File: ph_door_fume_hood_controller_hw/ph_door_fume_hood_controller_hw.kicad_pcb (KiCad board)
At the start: 2 copper layers, 145.7 x 133.3 mm, 249 parts, among them IC1 6N137, IC2 6N137, J1 Conn_01x03, J10 Conn_01x03, J11 Conn_01x02, J12 Conn_01x06, J13 Conn_01x02, J14 Conn_01x03, J15 Conn_01x03, J2 Conn_01x04, J3 CONN_01X04, J4 Conn_01x03, J5 Conn_01x03, J6 Conn_01x02, J7 Conn_01x06, J8 USB_OTG, J9 Conn_01x02, M1 DC-DC-24-12V-200mA, M2 MORSUN_485, Q1 C1815, Q10 A1015, Q11 Q_NMOS_GDS, Q2 Q_PMOS_GDS, Q3 Q_NMOS_GDS, Q4 Q_NMOS_GDS, Q5 C1815, Q6 Q_NMOS_GDS, Q7 Q_NMOS_GDS, Q8 C1815, Q9 Q_NMOS_GDS, U1 74HC123, U10 PC817, U11 MCP4725, U12 ASM1117-3V3, U13 PC817, U14 PC817, U15 LM358, U16 PC817, U17 PC817, U18 PC817, U19 PC817, U2 AD8601, U20 PC817, U21 PC817, U22 PC817, U23 PC817, U3 PC817, U4 PC817, U5 TB6600, U6 PC817, U7 STM32F103C8, U8 ASM1117, U9 XL4015, Y1 Crystal, Y2 32768Mhz

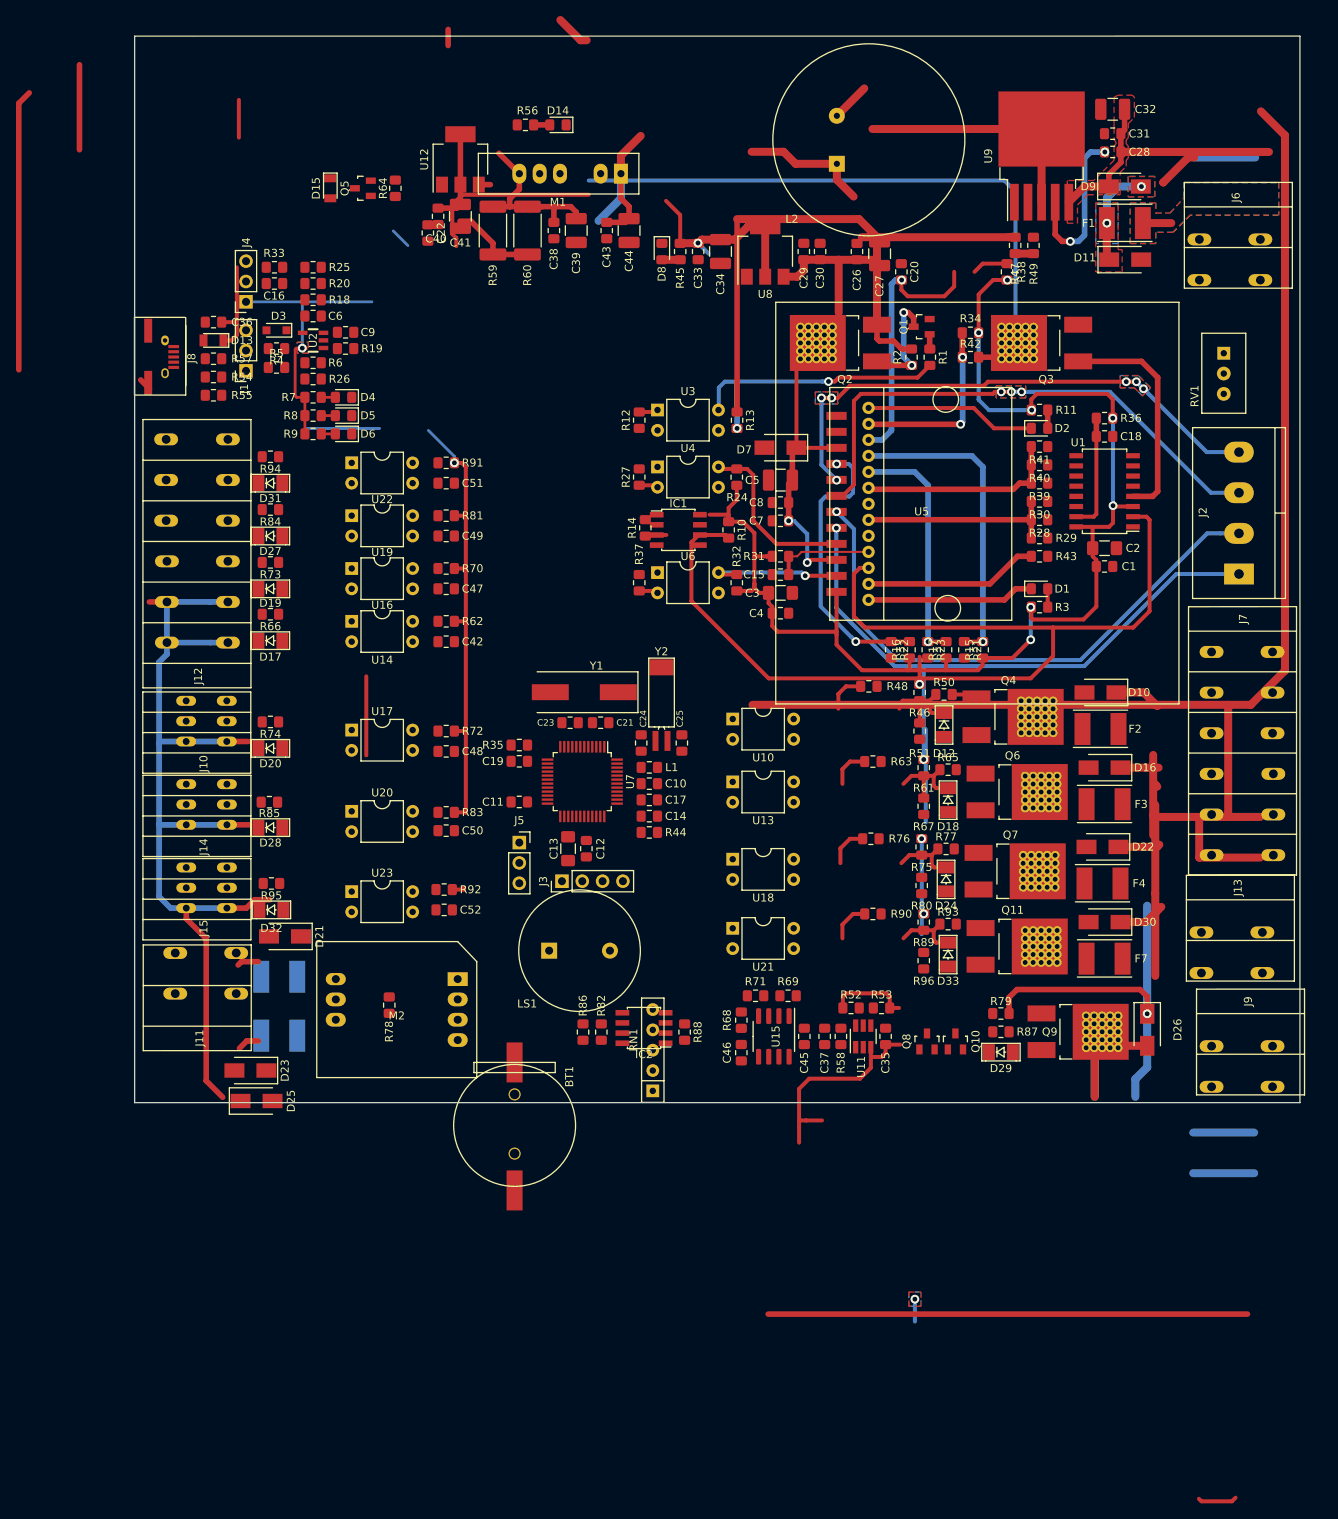
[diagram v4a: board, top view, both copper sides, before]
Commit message: door_fume_hood
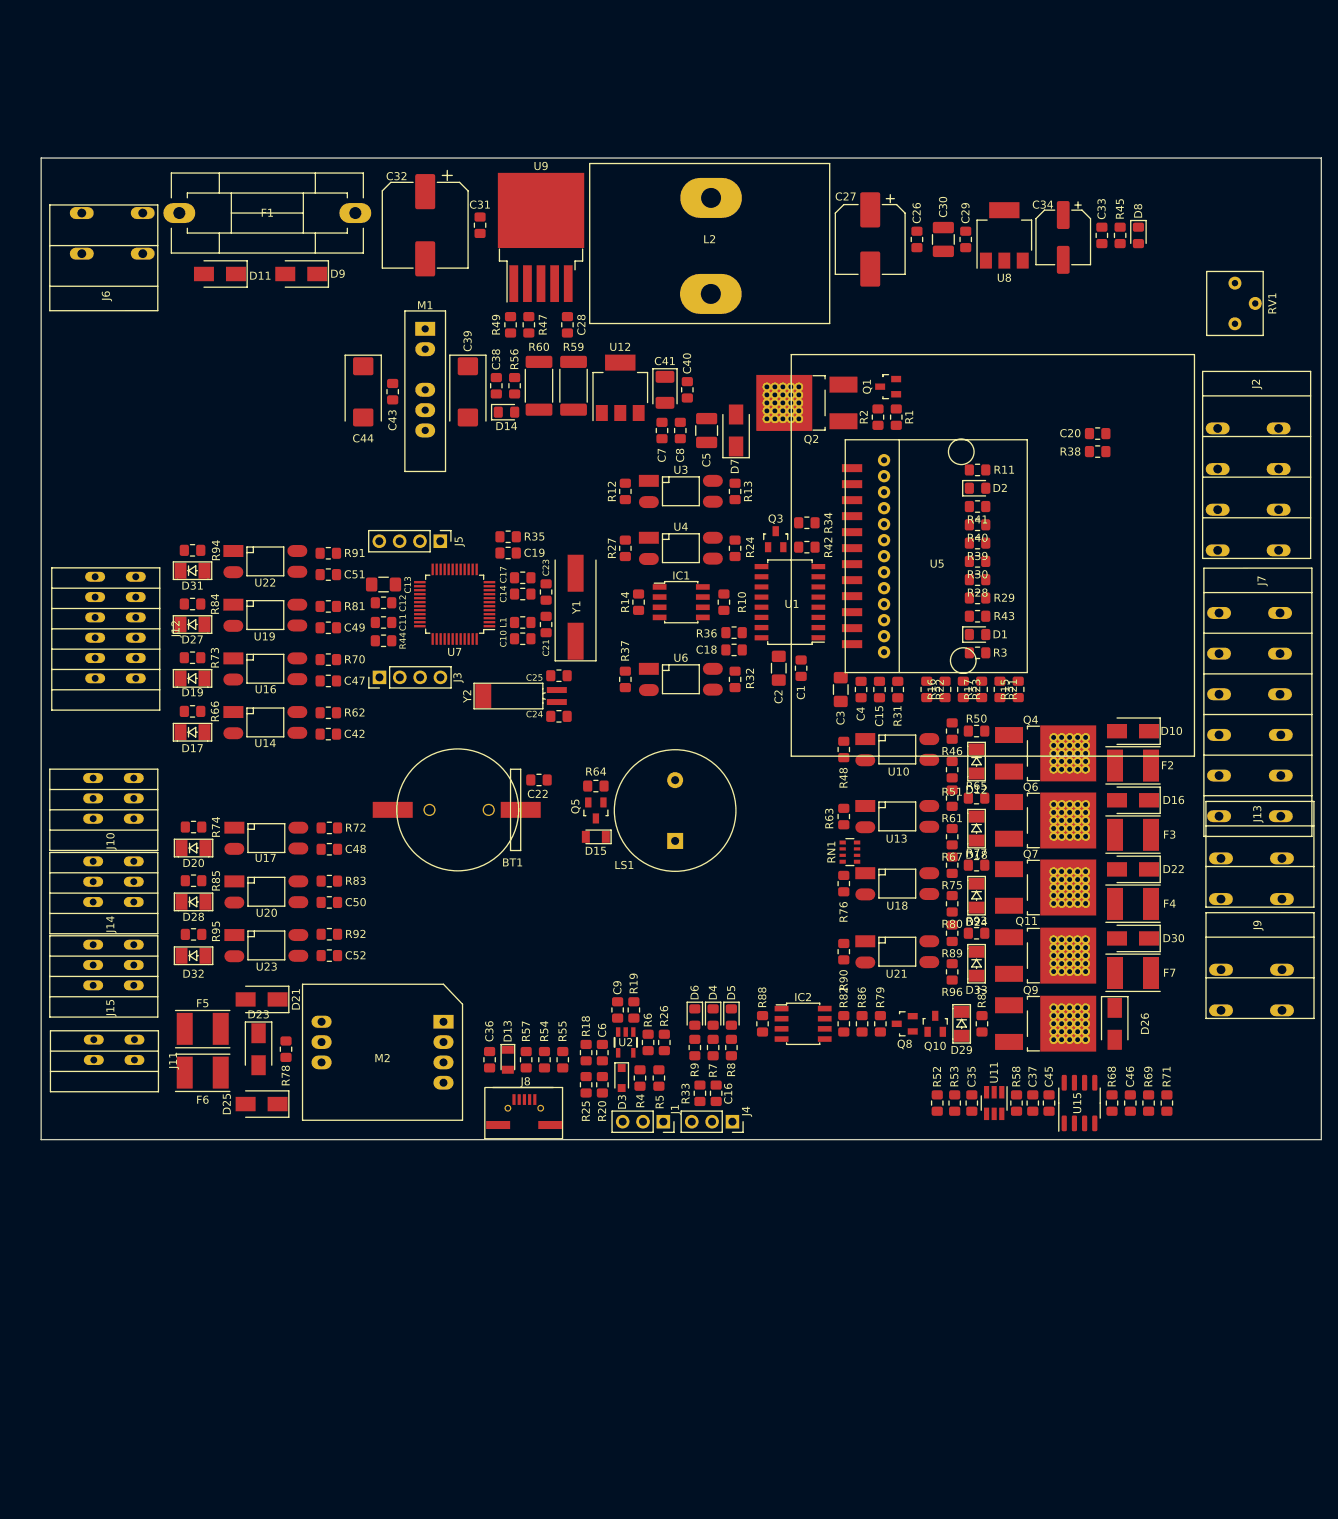
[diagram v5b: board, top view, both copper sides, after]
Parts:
- C27: footprint Capacitor_SMD:C_1210_3225Metric_Pad1.42x2.65mm_HandSolder -> Capacitor_SMD:CP_Elec_8x10.5
- C30: value 10uF -> 10uF/25V; footprint Capacitor_SMD:C_0805_2012Metric_Pad1.15x1.40mm_HandSolder -> Capacitor_SMD:C_1210_3225Metric_Pad1.42x2.65mm_HandSolder
- C32: value 220uF/50V -> 470uF/50V; footprint Capacitor_SMD:C_1210_3225Metric_Pad1.42x2.65mm_HandSolder -> Capacitor_SMD:CP_Elec_10x14.3
- C34: footprint Capacitor_SMD:C_1210_3225Metric_Pad1.42x2.65mm_HandSolder -> Capacitor_SMD:CP_Elec_6.3x5.4
- C39: value 330uF/25V -> 100uF/25V; footprint Capacitor_SMD:C_1210_3225Metric_Pad1.42x2.65mm_HandSolder -> Capacitor_Tantalum_SMD:CP_EIA-7343-20_Kemet-V_Pad2.25x2.55mm_HandSolder
- C41: value 47uF -> 100uF/10V; footprint Capacitor_SMD:C_1210_3225Metric_Pad1.42x2.65mm_HandSolder -> Capacitor_Tantalum_SMD:CP_EIA-3528-15_AVX-H_Pad1.50x2.35mm_HandSolder
- C44: value 330uF/25V -> 100uF/50V; footprint Capacitor_SMD:C_1210_3225Metric_Pad1.42x2.65mm_HandSolder -> Capacitor_Tantalum_SMD:CP_EIA-7343-31_Kemet-D_Pad2.25x2.55mm_HandSolder
- F1: footprint VinhTho_Lib:Fuse_SMD1812 -> VinhTho_Lib:Fuseholder5x20_horiz_SemiClosed_Casing10x25mm
- F5, F6: moved to F.Cu
- J11: footprint VinhTho_Lib:TerminalBlock_WAGO-236_2Stift_R5mm_2pol -> VinhTho_Lib:TerminalBlock_WAGO_2.54mm_2P
- J12: footprint VinhTho_Lib:TerminalBlock-WAGO-6P -> VinhTho_Lib:TerminalBlock_WAGO_2.54mm_6P
- J2: footprint VinhTho_Lib:Domino-5.08mm_4pol -> VinhTho_Lib:TerminalBlock_WAGO-236_2Stift_R5mm_4pol
- J5: value Conn_01x03 -> Conn_01x04; footprint Connector_PinSocket_2.54mm:PinSocket_1x03_P2.54mm_Vertical -> Connector_PinHeader_2.54mm:PinHeader_1x04_P2.54mm_Vertical
- L2: footprint VinhTho_Lib:L181-5A -> VinhTho_Lib:Inductor_5A
- Q3: value Q_NMOS_GDS -> Q_NMOS_GSD; footprint VinhTho_Lib:TO-252-2 -> VinhTho_Lib:SOT-23
- RN1: value R_Network04 -> R_Pack04; footprint Resistor_THT:R_Array_SIP5 -> Resistor_SMD:R_Array_Convex_4x0603
- RV1: footprint VinhTho_Lib:VR1 -> VinhTho_Lib:VR-3362P
- U10, U13, U14, U16, U17, U18, U19, U20, U21, U22, U23, U3, U4, U6: footprint Package_DIP:DIP-4_W7.62mm -> VinhTho_Lib:Optocoupler_SMD
- moved J6 147.3 mm to (66.0, 46.7), turned to 90 degrees
- moved J4 119.2 mm to (147.4, 155.2), turned to 270 degrees
- moved F1 118.2 mm to (78.2, 41.7), turned to 0 degrees
- moved R33 116.1 mm to (143.3, 151.7), turned to 270 degrees
- moved C16 115.3 mm to (145.3, 151.7), turned to 90 degrees
- moved D11 113.2 mm to (83.3, 49.3), turned to 180 degrees
- moved R25 107.7 mm to (129.1, 150.6), turned to 90 degrees
- moved J1 107.4 mm to (138.7, 155.2), turned to 270 degrees
- moved R20 106.5 mm to (131.1, 150.6), turned to 270 degrees
- moved J8 105.1 mm to (119.3, 153.6), turned to 0 degrees
- moved D9 103.5 mm to (93.5, 49.3), turned to 180 degrees
- moved D3 102.9 mm to (133.5, 149.8), turned to 270 degrees
- moved R4 101.9 mm to (135.8, 149.8), turned to 90 degrees
- moved R5 100.9 mm to (138.2, 149.8), turned to 90 degrees
- moved R18 100.1 mm to (129.1, 146.6), turned to 270 degrees
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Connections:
- J5 pad 1: /TX -> +3V3
- J5 pad 2: /RX -> GND
- J5 pad 3: GND -> /TX
- Q3 pad 2: Net-(Q3-Pad2) -> GNDPWR
- Q3 pad 3: GNDPWR -> Net-(Q3-Pad3)
- R42 pad 2: Net-(Q3-Pad2) -> Net-(Q3-Pad3)
- RN1 pad 2: /O4 -> GND
- RN1 pad 3: /O3 -> GND
- RN1 pad 4: /O2 -> GND
- RN1 pad 5: /O1 -> /O4
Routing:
- net +24V: track 583.2 -> 0.00 mm, vias 5 -> 0
- net +5V: track 272.2 -> 0.00 mm, vias 8 -> 0
- net +3V3: track 194.9 -> 0.00 mm, vias 3 -> 0
- net /CLK: track 126.0 -> 0.00 mm
- net +12V: track 116.1 -> 0.00 mm
- net Net-(J2-Pad2): track 71.0 -> 0.00 mm, vias 1 -> 0
- net Net-(J2-Pad1): track 68.1 -> 0.00 mm, vias 1 -> 0
- net Net-(J2-Pad4): track 67.7 -> 0.00 mm, vias 6 -> 0
- net Net-(J2-Pad3): track 67.0 -> 0.00 mm, vias 3 -> 0
- net Net-(C5-Pad1): track 41.2 -> 0.00 mm, vias 2 -> 0
- net /M1: track 39.1 -> 0.00 mm, vias 1 -> 0
- net GND: track 36.7 -> 0.00 mm
- net /PWR_STEP: track 36.2 -> 0.00 mm, vias 2 -> 0
- net /M2: track 35.9 -> 0.00 mm, vias 2 -> 0
- net Net-(L2-Pad2): track 35.1 -> 0.00 mm
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- removed copper zone on F.Cu, net +24V
- removed copper zone on B.Cu, net +3V3
- removed copper zone on F.Cu, net +3V3
- removed copper zone on B.Cu, net Net-(D11-Pad1)
- removed copper zone on F.Cu, net Net-(D11-Pad1)
- removed copper zone on B.Cu, net Net-(F1-Pad1)
- removed copper zone on F.Cu, net Net-(F1-Pad1)
- removed copper zone on B.Cu, net Net-(J2-Pad3)
- removed copper zone on F.Cu, net Net-(J2-Pad3)
- removed copper zone on B.Cu, net Net-(J2-Pad4)
- removed copper zone on F.Cu, net Net-(J2-Pad4)
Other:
- board size 145.7 x 133.3 mm -> 160 x 122.7 mm

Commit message: Layoutting door fume
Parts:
- removed R25, R5: 0R, Resistor_SMD:R_0805_2012Metric_Pad1.15x1.40mm_HandSolder
- J13: footprint VinhTho_Lib:TerminalBlock_WAGO-236_2Stift_R5mm_2pol -> VinhTho_Lib:TerminalBlock_WAGO_2.54mm_2P
- J7: footprint VinhTho_Lib:TerminalBlock-WAGO-6P -> VinhTho_Lib:TerminalBlock_WAGO_2.54mm_6P
- J9: footprint VinhTho_Lib:TerminalBlock_WAGO-236_2Stift_R5mm_2pol -> Connector_PinSocket_2.54mm:PinSocket_1x02_P2.54mm_Vertical
- Q11, Q4, Q6, Q7, Q9: value Q_NMOS_GDS -> Q_NMOS_GSD; footprint VinhTho_Lib:TO-252-2 -> VinhTho_Lib:SOT-23
- moved J9 100.0 mm to (116.1, 137.9)
- moved R71 94.6 mm to (108.7, 135.1), turned to 180 degrees
- moved R69 92.9 mm to (108.7, 132.6), turned to 180 degrees
- moved U15 78.3 mm to (114.9, 133.2), turned to 0 degrees
- moved C46 78.0 mm to (121.2, 135.1), turned to 180 degrees
- moved R68 76.4 mm to (121.2, 132.6), turned to 0 degrees
- moved C45 75.9 mm to (114.9, 129.0), turned to 180 degrees
- moved R53 70.9 mm to (110.2, 124.4), turned to 180 degrees
- moved C37 70.7 mm to (120.1, 124.6), turned to 180 degrees
- moved U11 70.4 mm to (115.1, 125.9), turned to 180 degrees
- moved C35 69.0 mm to (115.1, 123.1), turned to 0 degrees
- moved R58 68.0 mm to (120.1, 126.6), turned to 0 degrees
- moved R52 68.0 mm to (110.2, 126.6), turned to 180 degrees
- moved J15 55.9 mm to (68.9, 81.2)
- moved R95 49.0 mm to (80.0, 82.8)
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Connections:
- C36 pad 1: +5V -> +5VA
- D13 pad 1: +5V -> +5VA
- D15 pad 1: +5V -> +3V3
- LS1 pad 1: +5V -> +3V3
- Q11 pad 2: Net-(D30-Pad2) -> GNDPWR
- Q11 pad 3: GNDPWR -> Net-(D30-Pad2)
- Q4 pad 2: Net-(D10-Pad2) -> GNDPWR
- Q4 pad 3: GNDPWR -> Net-(D10-Pad2)
- Q6 pad 2: Net-(D16-Pad2) -> GNDPWR
- Q6 pad 3: GNDPWR -> Net-(D16-Pad2)
- Q7 pad 2: Net-(D22-Pad2) -> GNDPWR
- Q7 pad 3: GNDPWR -> Net-(D22-Pad2)
- Q9 pad 2: Net-(D26-Pad2) -> GNDPWR
- Q9 pad 3: GNDPWR -> Net-(D26-Pad2)
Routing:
- net +3V3: track 0.00 -> 403.5 mm, vias 0 -> 14
- net +24V: track 0.00 -> 360.0 mm, vias 0 -> 12
- net +5V: track 0.00 -> 215.9 mm, vias 0 -> 3
- net +12V: track 0.00 -> 167.1 mm, vias 0 -> 3
- net +12VA: track 0.00 -> 142.5 mm, vias 0 -> 2
- net /O4: track 0.00 -> 106.1 mm, vias 0 -> 2
- net /O3: track 0.00 -> 99.5 mm, vias 0 -> 2
- net /O1: track 0.00 -> 90.9 mm, vias 0 -> 2
- net /O2: track 0.00 -> 89.5 mm, vias 0 -> 2
- net /PWM: track 0.00 -> 84.8 mm, vias 0 -> 2
- net Net-(J2-Pad2): track 0.00 -> 83.3 mm, vias 0 -> 1
- net Net-(J2-Pad1): track 0.00 -> 83.0 mm, vias 0 -> 1
- net Net-(J2-Pad4): track 0.00 -> 79.8 mm, vias 0 -> 1
- net /LED3: track 0.00 -> 79.0 mm, vias 0 -> 2
- net Net-(J2-Pad3): track 0.00 -> 75.7 mm, vias 0 -> 1
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- added copper zone on B.Cu, net +3V3
- added copper zone on F.Cu, net +3V3
- added copper zone on B.Cu, net GND
- added copper zone on F.Cu, net GND
- added copper zone on B.Cu, net GNDPWR
- added copper zone on F.Cu, net GNDPWR
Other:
- board size 160 x 122.7 mm -> 160 x 105.2 mm
- net class Default: clearance 0.25 -> 0.2
- net class Users added: clearance 0.3, trace_width 0.254, via_dia 1.1, via_drill 0.6
- rule trace_clearance: 0.25 -> 0.2

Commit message: edit mass
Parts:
- moved R44 1.02 mm to (113.0, 92.5)
- moved C10 0.89 mm to (115.3, 92.5)
- moved J5 0.76 mm to (109.7, 76.8)
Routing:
- net +24V: track 360.0 -> 510.8 mm
- net /SCL: track 2.77 -> 88.0 mm, vias 0 -> 2
- net /SDA: track 2.64 -> 81.6 mm, vias 0 -> 2
- net +3V3: track 403.5 -> 426.2 mm, vias 14 -> 17
- net GND: track 1.65 -> 19.6 mm, vias 3 -> 55
- net Net-(C19-Pad1): track 12.8 -> 1.95 mm
- net /ss1: track 59.0 -> 69.7 mm
- net /ss2: track 49.2 -> 55.9 mm
- net +5V: track 215.9 -> 221.3 mm
- net /ss3: track 42.0 -> 46.3 mm
- net /TQ: track 23.6 -> 21.0 mm
- net Net-(Q3-Pad1): track 12.7 -> 10.9 mm
- net GNDPWR: track 0.00 -> 1.52 mm, vias 0 -> 30
- net /in4: track 73.3 -> 74.4 mm
- net /ENA: track 26.2 -> 25.3 mm
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
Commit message: Layout Fume_hood is finished
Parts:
- moved R35 4.31 mm to (125.6, 74.0), turned to 0 degrees
- moved C19 4.27 mm to (125.6, 76.1), turned to 180 degrees
- moved C42 0.62 mm to (96.6, 78.2)
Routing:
- net GND: track 19.6 -> 45.3 mm, vias 55 -> 67
- net Net-(C19-Pad1): track 1.95 -> 19.1 mm
- net /LED2: track 61.6 -> 64.9 mm
- net Net-(BT1-Pad1): track 20.7 -> 23.9 mm
- net /O1: track 90.9 -> 87.6 mm
- net +3V3: track 426.2 -> 429.2 mm, vias 17 -> 20
- net Net-(C14-Pad2): track 31.5 -> 34.2 mm
- net /LED1: track 57.1 -> 59.4 mm
- net /LED3: track 79.3 -> 77.1 mm
- net /O2: track 89.5 -> 88.0 mm
- net /ss3: track 46.3 -> 47.6 mm
- net /O4: track 106.1 -> 104.9 mm
- net /analog2: track 51.7 -> 52.8 mm
- net /O3: track 99.5 -> 98.5 mm
- net /485_RX: track 39.2 -> 38.6 mm
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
